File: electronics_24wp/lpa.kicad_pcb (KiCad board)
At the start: 2 copper layers, 143 x 74 mm, 85 parts, among them CON1 BARREL_JACK, IC1 ATMEGA328-A, P2 CONN_3X2, U1 SD_CARD, U2 AP1509, U3 TLC5941, U4 TLC5941, U5 TLC5941, X1 CRYSTAL_SMD

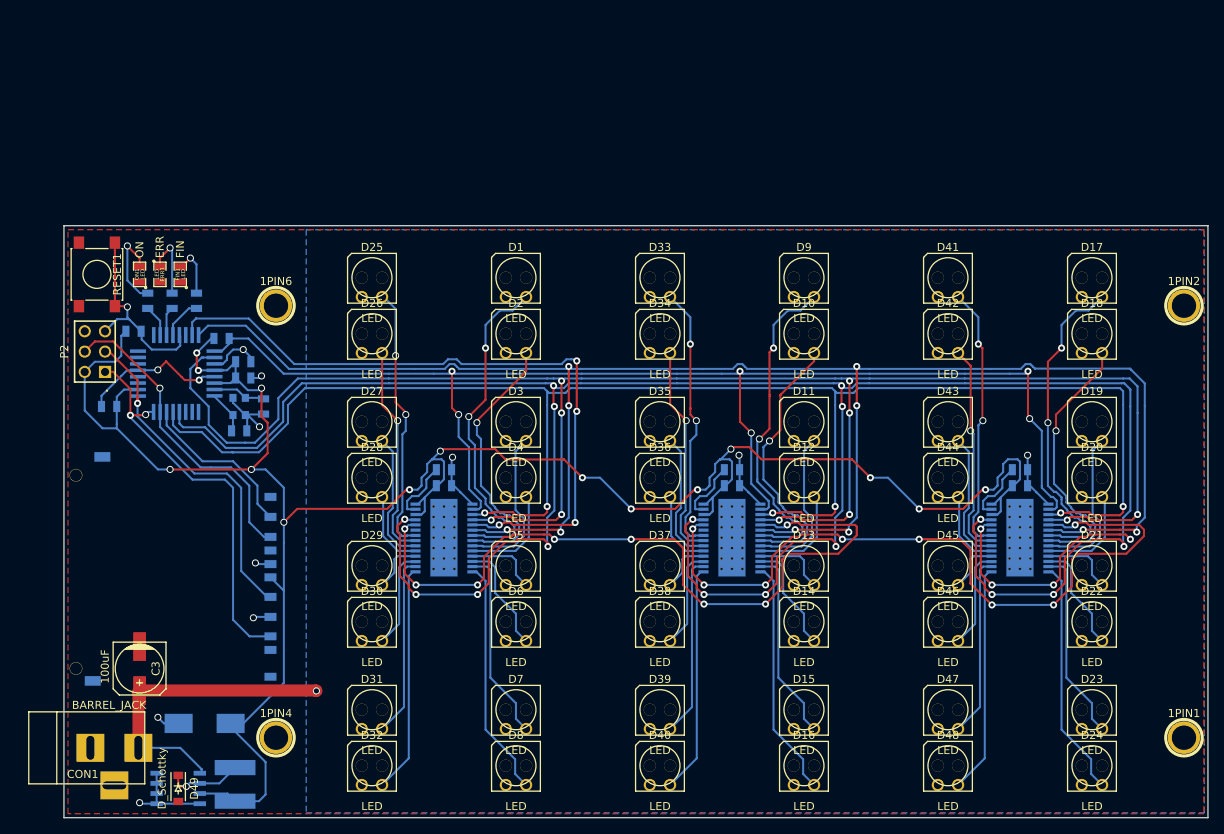
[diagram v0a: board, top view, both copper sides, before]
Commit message: Moved power circuit to the back entirely.
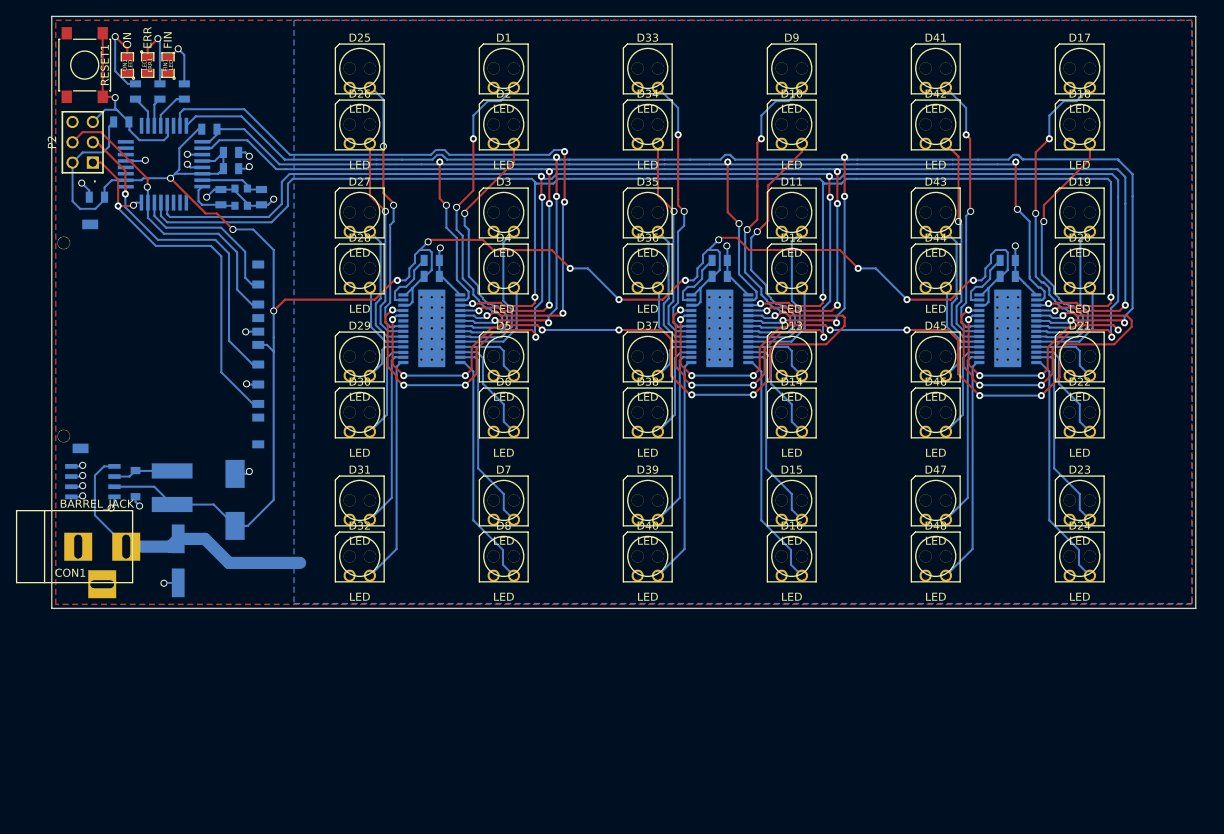
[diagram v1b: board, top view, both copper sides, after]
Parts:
- removed 1PIN1, 1PIN2, 1PIN4, 1PIN6: P***, 1pin
- C3, D49: moved to B.Cu
- moved U2 39.8 mm to (70.6, 126.5)
- moved D49 38.5 mm to (75.9, 126.7)
- moved L1 37.9 mm to (80.5, 127.3)
- moved C10 29.3 mm to (86.6, 90.9), turned to 270 degrees
- moved U1 29.1 mm to (67.0, 108.0)
- moved C5 28.2 mm to (88.4, 128.8), turned to 270 degrees
- moved C11 26.2 mm to (87.9, 85.3)
- moved C6 26.2 mm to (113.0, 100.8)
- moved C7 26.2 mm to (149.0, 100.8)
- moved C8 26.2 mm to (185.0, 100.8)
- moved D1 26.2 mm to (122.0, 74.8)
- moved D10 26.2 mm to (158.0, 81.8)
- moved D11 26.2 mm to (158.0, 92.8)
- moved D12 26.2 mm to (158.0, 99.8)
- moved D13 26.2 mm to (158.0, 110.8)
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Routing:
- net /tlcs_1-3/SCLK: track 219.2 -> 203.0 mm
- net GND: track 76.6 -> 60.5 mm, vias 12 -> 21
- net /tlcs_1-3/VCC: track 281.7 -> 267.0 mm, vias 15 -> 12
- net /MISO: track 49.2 -> 46.8 mm
- net Net-(C9-Pad2): track 6.34 -> 8.51 mm
- net Net-(C10-Pad2): track 5.42 -> 7.53 mm
- net /tlcs_1-3/GSCLK: track 290.9 -> 288.8 mm
- net /tlcs_1-3/XLAT: track 203.0 -> 201.1 mm
- net /tlcs_1-3/VIN: track 39.7 -> 37.8 mm, vias 1 -> 0
- net /SCK: track 44.5 -> 43.0 mm
- net /MOSI: track 39.4 -> 38.3 mm
- net Net-(D49-Pad1): track 9.32 -> 8.31 mm, vias 1 -> 0
- net /SS: track 20.7 -> 20.1 mm

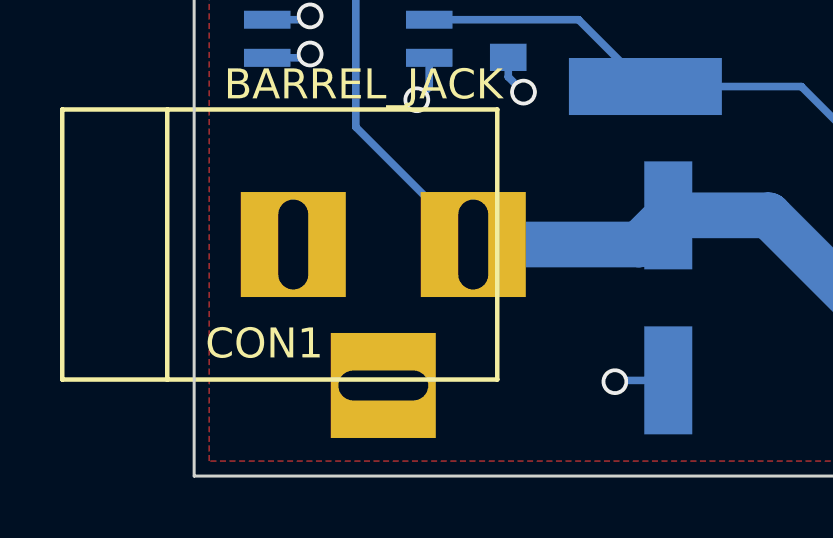
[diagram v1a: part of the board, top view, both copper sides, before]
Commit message: Changed barrel jack pads to circular.
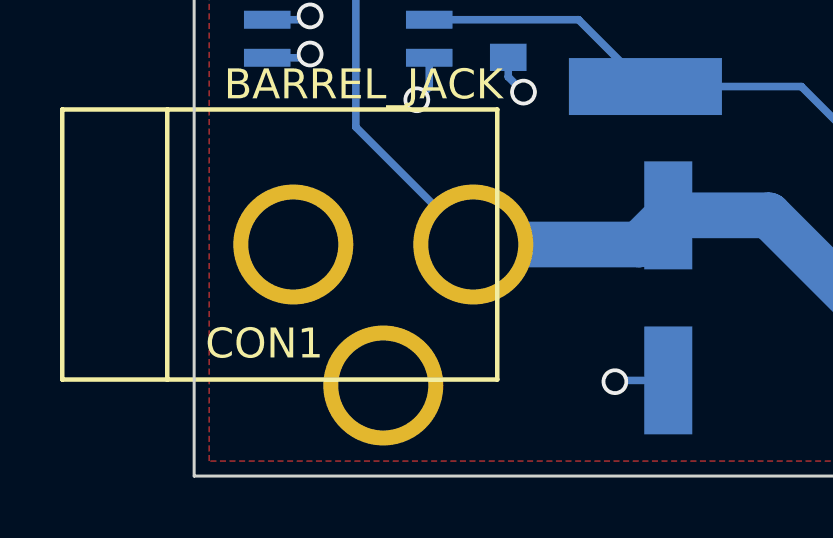
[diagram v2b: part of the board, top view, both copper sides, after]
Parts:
- CON1: footprint Connect:BARREL_JACK -> LPA_parts:BARREL_JACK_CIRCULAR_PADS
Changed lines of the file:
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@@
     (links 266)
     (no_connects 0)
-    (area 62.274379 88.399999 214.600001 176.600001)
+    (area 60.750379 62.237999 213.076001 150.438001)
     (thickness 1.6)
     (drawings 60)
@@
     )
   )
-  (module Connect:BARREL_JACK (layer F.Cu)
-    (at 68.58 134.62)
-    (descr "DC Barrel Jack")
-    (tags "Power Jack")
-    (fp_text reference CON1 (at -0.762 3.302 180) (layer F.SilkS)
-      (effects (font (size 1 1) (thickness 0.15)))
-    )
-    (fp_text value BARREL_JACK (at 2.54 -5.334) (layer F.SilkS)
-      (effects (font (size 1 1) (thickness 0.15)))
-    )
-    (fp_line (start -4.0005 -4.50088) (end -4.0005 4.50088) (layer F.SilkS) (width 0.15))
-    (fp_line (start -7.50062 -4.50088) (end -7.50062 4.50088) (layer F.SilkS) (width 0.15))
-    (fp_line (start -7.50062 4.50088) (end 7.00024 4.50088) (layer F.SilkS) (width 0.15))
-    (fp_line (start 7.00024 4.50088) (end 7.00024 -4.50088) (layer F.SilkS) (width 0.15))
-    (fp_line (start 7.00024 -4.50088) (end -7.50062 -4.50088) (layer F.SilkS) (width 0.15))
-    (pad 1 thru_hole rect (at 6.20014 0) (size 3.50012 3.50012) (drill oval 1.00076 2.99974) (layers *.Cu *.Mask F.SilkS)
-      (net 15 /tlcs_1-3/VIN))
-    (pad 2 thru_hole rect (at 0.20066 0) (size 3.50012 3.50012) (drill oval 1.00076 2.99974) (layers *.Cu *.Mask F.SilkS)
-      (net 17 GND))
-    (pad 3 thru_hole rect (at 3.2004 4.699) (size 3.50012 3.50012) (drill oval 2.99974 1.00076) (layers *.Cu *.Mask F.SilkS)
-      (net 17 GND))
-  )
   (module Capacitors_SMD:c_elec_6.3x7.7 (layer B.Cu)
     (at 81.28 136.398 90)
@@
     )
   )
+  (module LPA_parts:BARREL_JACK_CIRCULAR_PADS (layer F.Cu)
+    (at 68.58 134.62)
+    (descr "DC Barrel Jack")
+    (tags "Power Jack")
+    (fp_text reference CON1 (at -0.762 3.302 180) (layer F.SilkS)
+      (effects (font (size 1 1) (thickness 0.15)))
+    )
+    (fp_text value BARREL_JACK (at 2.54 -5.334) (layer F.SilkS)
+      (effects (font (size 1 1) (thickness 0.15)))
+    )
+    (fp_line (start -4.0005 -4.50088) (end -4.0005 4.50088) (layer F.SilkS) (width 0.15))
+    (fp_line (start -7.50062 -4.50088) (end -7.50062 4.50088) (layer F.SilkS) (width 0.15))
+    (fp_line (start -7.50062 4.50088) (end 7.00024 4.50088) (layer F.SilkS) (width 0.15))
+    (fp_line (start 7.00024 4.50088) (end 7.00024 -4.50088) (layer F.SilkS) (width 0.15))
+    (fp_line (start 7.00024 -4.50088) (end -7.50062 -4.50088) (layer F.SilkS) (width 0.15))
+    (pad 1 thru_hole circle (at 6.20014 0) (size 4 4) (drill 3) (layers *.Cu *.Mask F.SilkS)
+      (net 15 /tlcs_1-3/VIN))
+    (pad 2 thru_hole circle (at 0.20066 0) (size 4 4) (drill 3) (layers *.Cu *.Mask F.SilkS)
+      (net 17 GND))
+    (pad 3 thru_hole circle (at 3.2004 4.699) (size 4 4) (drill 2.99974) (layers *.Cu *.Mask F.SilkS)
+      (net 17 GND))
+  )
   (gr_text . (at 70.866 88.392) (layer F.SilkS)

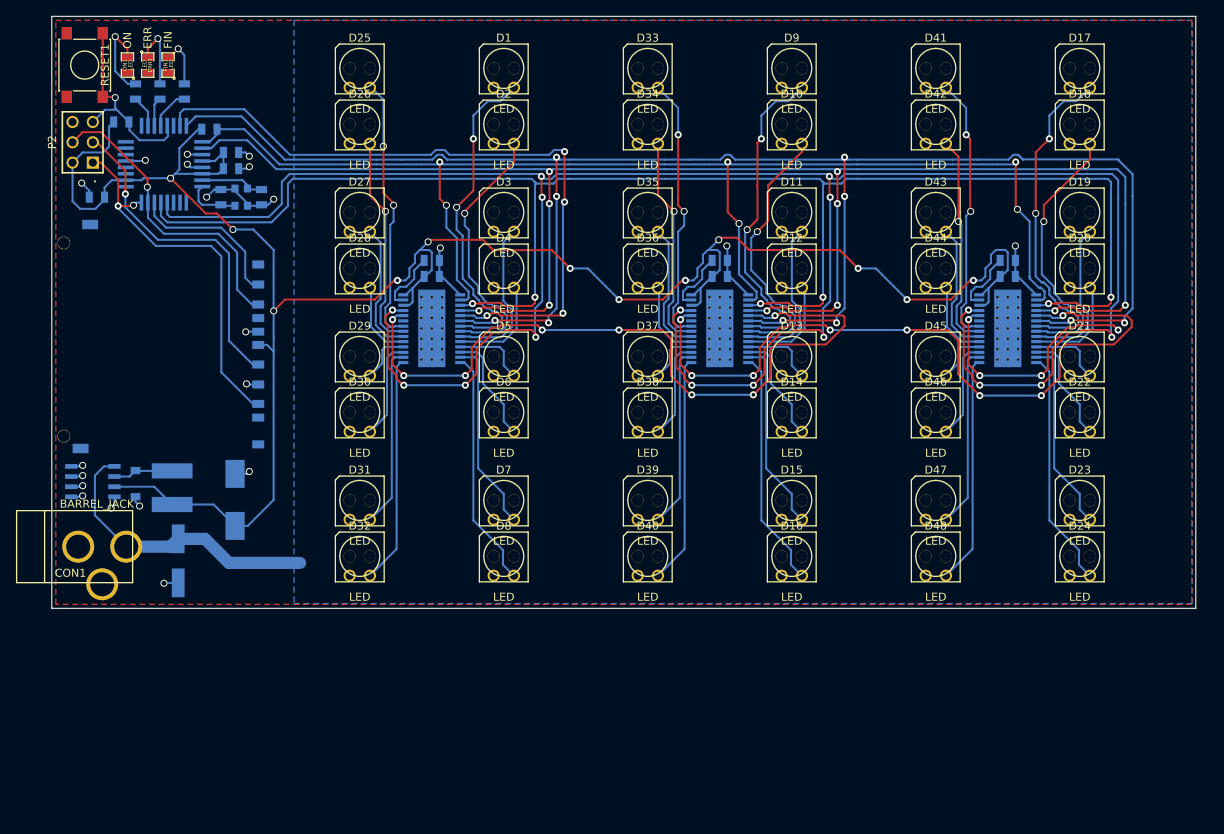
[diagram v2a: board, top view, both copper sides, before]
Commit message: Small modifications to PCB silkscreen.
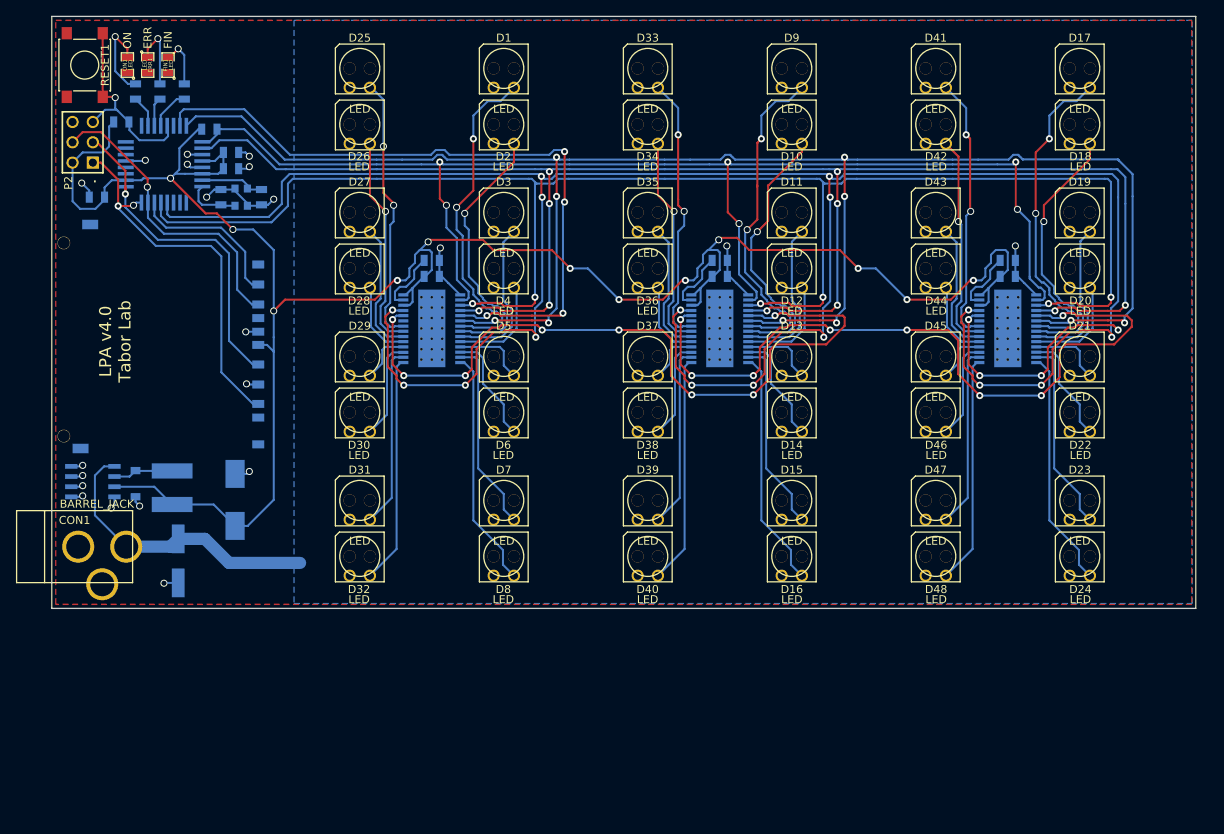
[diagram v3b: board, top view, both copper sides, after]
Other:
- board text added: "LPA v4.0 Tabor Lab"
